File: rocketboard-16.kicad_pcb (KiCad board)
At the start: 2 copper layers, 86.2 x 105.8 mm, 128 parts, among them J1 SWD, K1 MX_RGB, K10 MX_RGB, K11 MX_RGB, K12 MX_RGB, K13 MX_RGB, K14 MX_RGB, K15 MX_RGB, K16 MX_RGB, K2 MX_RGB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

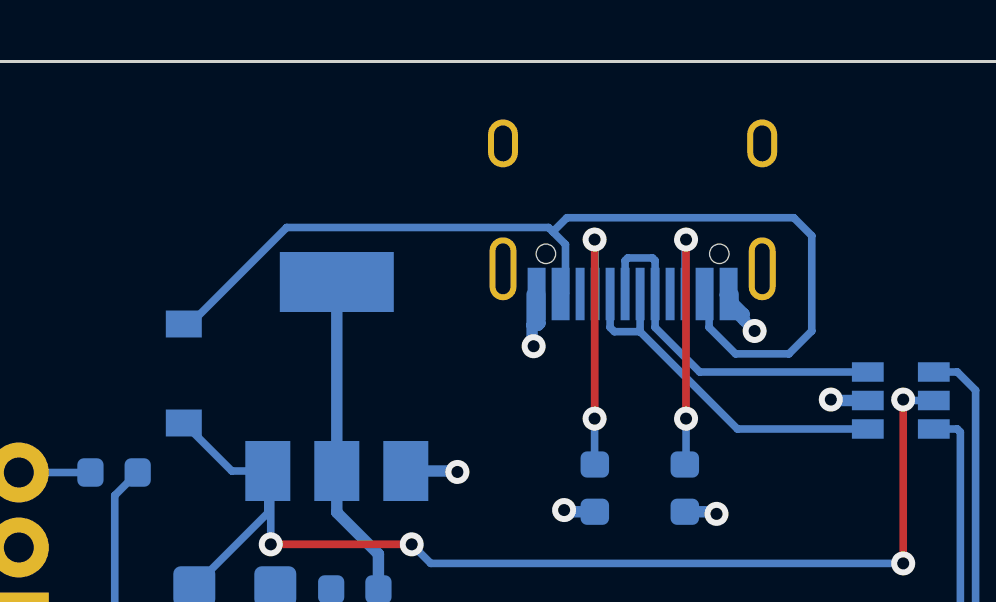
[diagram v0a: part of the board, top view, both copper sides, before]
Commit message: Changed the USB type C connector for one that fits the footprint of the LCSC part - had to adjust clearance on some pins for DRC and re-route some connections
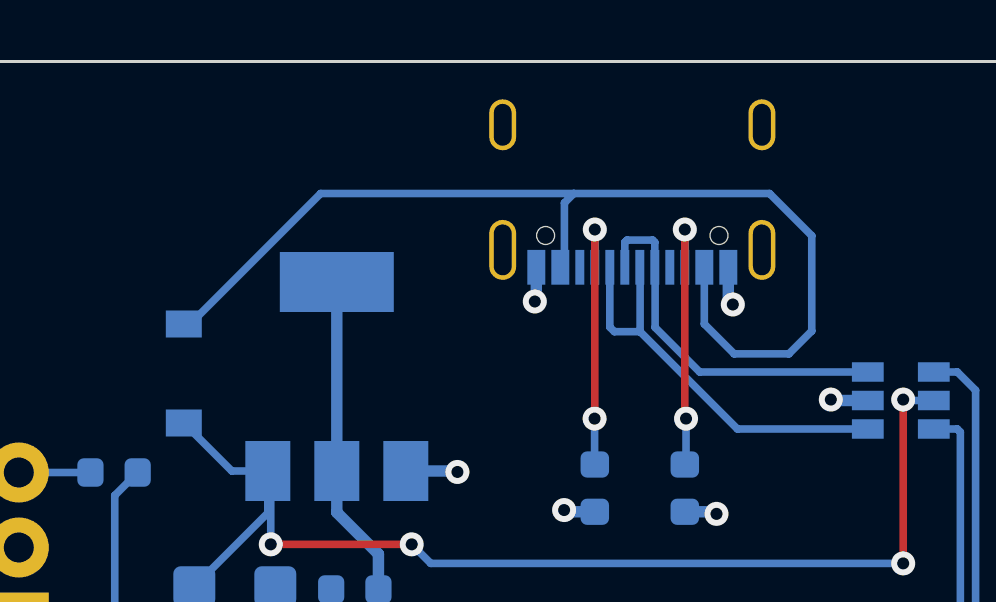
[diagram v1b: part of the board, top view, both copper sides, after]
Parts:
- P1: footprint seth-connectors:USB_C_U262-161N-4BVC11 -> Connector_USB:USB_C_Receptacle_Palconn_UTC16-G
- moved P1 0.25 mm to (123.0, 49.9)
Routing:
- net GND: track 170.5 -> 167.3 mm
- net Net-(P1-PadA7): track 12.4 -> 14.2 mm
- net Net-(D17-Pad2): track 34.0 -> 35.3 mm

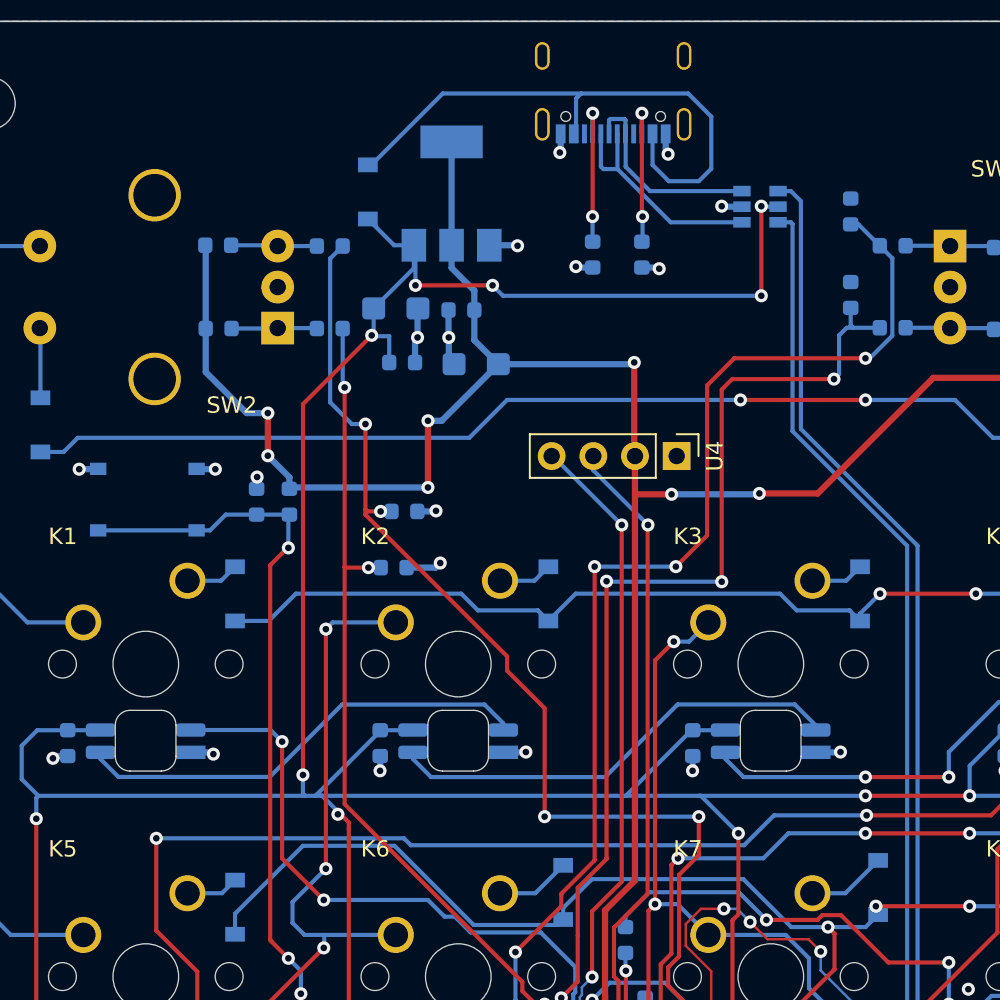
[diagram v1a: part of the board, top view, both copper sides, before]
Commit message: Added in a level shifting circuit for the LED signal (needs 5v sig, not 3.3v), added a 10uf cap on the 5v line for smoothing out possible spikey power draw from LEDs, and added test points on +5v, VCC, and GND
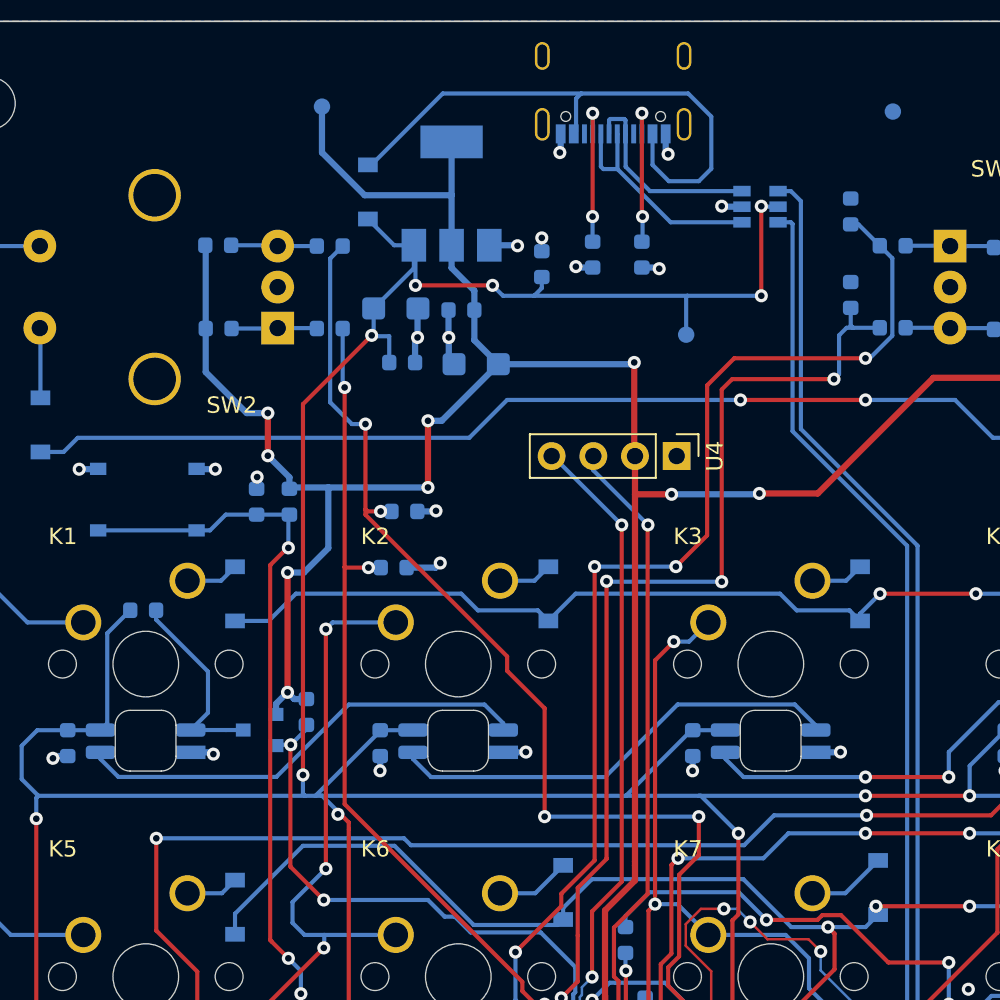
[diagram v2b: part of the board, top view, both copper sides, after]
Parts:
- added C36: 10u, Capacitor_SMD:C_0603_1608Metric, B.Cu at (118.7, 60.3)
- added Q1: BSS138, Package_TO_SOT_SMD:SOT-23, B.Cu at (101.5, 88.7)
- added R18: 10k, Resistor_SMD:R_0603_1608Metric, B.Cu at (104.3, 87.6)
- added R19: 10k, Resistor_SMD:R_0603_1608Metric, B.Cu at (94.4, 81.4)
- added TP1: TestPoint, TestPoint:TestPoint_Pad_D1.0mm, B.Cu at (127.5, 64.6)
- added TP2: TestPoint, TestPoint:TestPoint_Pad_D1.0mm, B.Cu at (105.3, 50.7)
- added TP3: TestPoint, TestPoint:TestPoint_Pad_D1.0mm, B.Cu at (140.1, 51.0)
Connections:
- K1 pad 3: LED_SIG -> LED_SHIFTED
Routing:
- net VCC: track 223.4 -> 252.2 mm, vias 13 -> 15
- net LED_SHIFTED: track 0.00 -> 12.2 mm
- net +5V: track 434.5 -> 446.3 mm
- net LED_SIG: track 39.6 -> 35.9 mm
- net GND: track 167.3 -> 168.1 mm, vias 67 -> 68
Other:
- board text added: "+5v"
- board text added: "GND"
- board text added: "VCC"

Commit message: Updated design to include 10k resistors between boot select jumpers and MCU
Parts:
- added R20: 10k, Resistor_SMD:R_0603_1608Metric, B.Cu at (145.4, 113.3)
- added R21: 10k, Resistor_SMD:R_0603_1608Metric, B.Cu at (142.4, 124.5)
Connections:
- JP1 pad 2: BOOT1 -> Net-(JP1-Pad2)
- JP2 pad 2: BOOT0 -> Net-(JP2-Pad2)
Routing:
- net BOOT0: track 40.6 -> 20.8 mm, vias 4 -> 2
- net Net-(JP2-Pad2): track 0.00 -> 18.3 mm, vias 0 -> 2
- net BOOT1: track 40.9 -> 34.4 mm, vias 6 -> 4
- net Net-(JP1-Pad2): track 0.00 -> 4.95 mm, vias 0 -> 2
